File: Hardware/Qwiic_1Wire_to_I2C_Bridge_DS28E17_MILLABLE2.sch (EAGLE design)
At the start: 20 parts, among them J1 RJ45, J2 RJ45, J3 RJ11, J4 RJ11

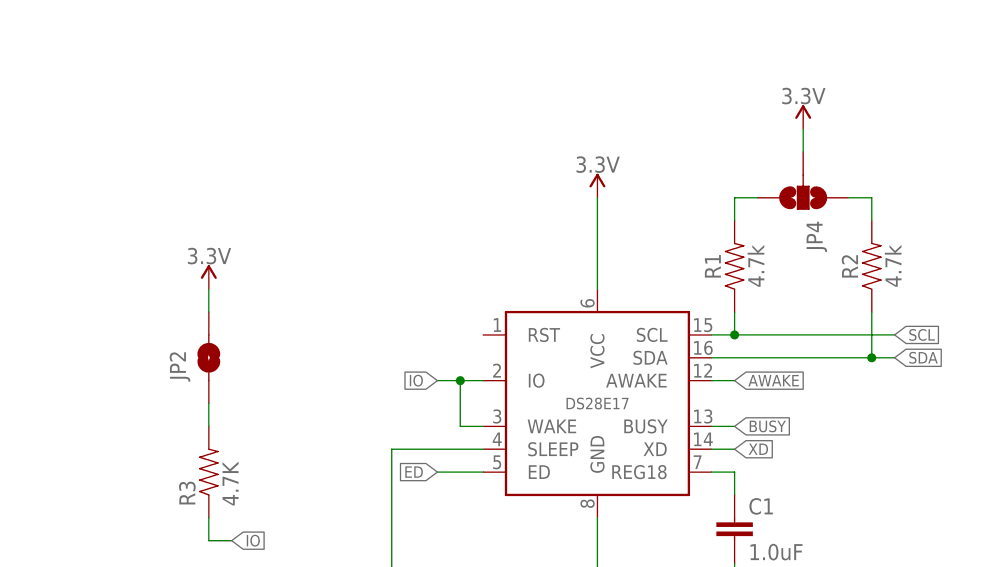
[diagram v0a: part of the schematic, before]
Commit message: Routed more on production layout
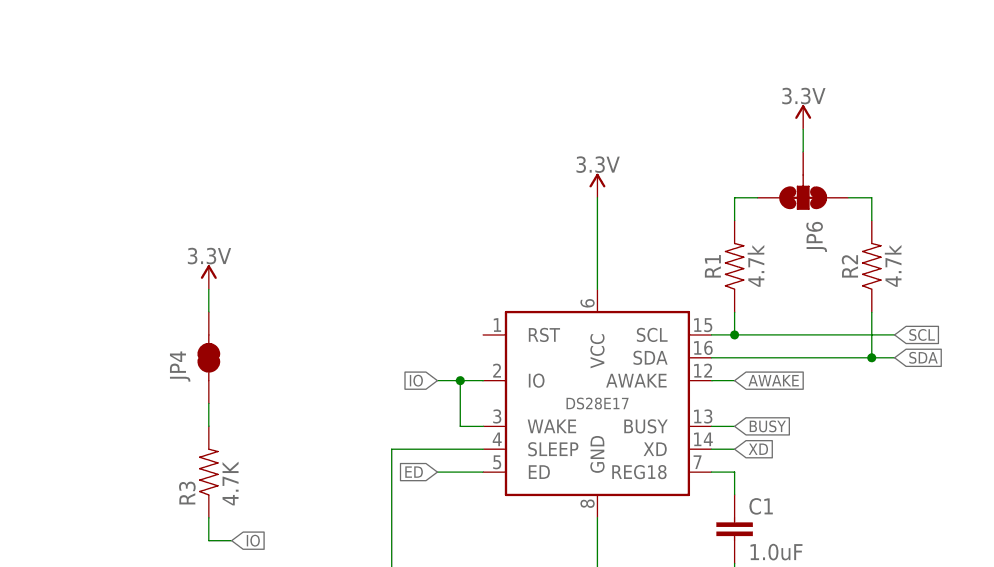
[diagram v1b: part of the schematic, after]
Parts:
- removed JP2: JUMPER-SMT_2_NO_NO-SILK, SparkFun-Jumpers:JUMPER-SMT_2_NO_NO-SILK
- added JP6: JUMPER-SMT_3_2-NC_TRACE_NO-SILK, SparkFun-Jumpers:JUMPER-SMT_3_2-NC_TRACE_NO-SILK
- JP4: value JUMPER-SMT_3_NO_NO-SILK -> JUMPER-SMT_2_NC_TRACE_NO-SILK; device SparkFun-Jumpers:JUMPER-SMT_3_NO_NO-SILK -> SparkFun-Jumpers:JUMPER-SMT_2_NC_TRACE_NO-SILK
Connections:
- net 3.3V: now also JP6.2; no longer JP2.2
- net N$2: now also JP4.1; no longer JP2.1
- net N$3: now also JP6.1; no longer JP4.1
- net N$4: now also JP6.3; no longer JP4.3
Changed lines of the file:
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@@
 <part name="R3" library="SparkFun-Resistors" deviceset="4.7KOHM-1/10W-1%(0603)" device="" value="4.7K"/>
 <part name="P+1" library="SparkFun" deviceset="VCC" device="" value="3.3V"/>
+<part name="JP4" library="SparkFun-Jumpers" deviceset="JUMPER-SMT_2_NC_TRACE" device="_NO-SILK" value=""/>
 <part name="SUPPLY4" library="SparkFun-PowerSymbols" deviceset="3.3V" device=""/>
 <part name="SUPPLY5" library="SparkFun-PowerSymbols" deviceset="3.3V" device=""/>
+<part name="JP6" library="SparkFun-Jumpers" deviceset="JUMPER-SMT_3_2-NC_TRACE" device="_NO-SILK" value=""/>
 <part name="J1" library="SparkFun-Connectors" deviceset="RJ45-8" device="" value="RJ45"/>
 <part name="J3" library="SparkFun-Connectors" deviceset="RJ11-6" device="" value="RJ11"/>
@@
 <part name="GND7" library="SparkFun-PowerSymbols" deviceset="GND" device=""/>
 <part name="SUPPLY3" library="SparkFun-PowerSymbols" deviceset="3.3V" device=""/>
-<part name="JP2" library="SparkFun-Jumpers" deviceset="JUMPER-SMT_2_NO" device="_NO-SILK" value=""/>
-<part name="JP4" library="SparkFun-Jumpers" deviceset="JUMPER-SMT_3_NO" device="_NO-SILK" value=""/>
 </parts>
 <sheets>
@@
 <instance part="R3" gate="G$1" x="78.74" y="114.3" rot="R90"/>
 <instance part="P+1" gate="1" x="45.72" y="127"/>
+<instance part="JP4" gate="G$1" x="78.74" y="127" rot="R90"/>
 <instance part="SUPPLY4" gate="G$1" x="78.74" y="134.62"/>
 <instance part="SUPPLY5" gate="G$1" x="144.78" y="152.4"/>
+<instance part="JP6" gate="G$1" x="144.78" y="144.78" rot="R270"/>
 <instance part="J1" gate="JP1" x="25.4" y="119.38" rot="R180"/>
 <instance part="J3" gate="G$1" x="17.78" y="96.52"/>
@@
 <instance part="GND7" gate="1" x="190.5" y="55.88"/>
 <instance part="SUPPLY3" gate="G$1" x="190.5" y="73.66"/>
-<instance part="JP2" gate="G$1" x="78.74" y="127" rot="R90"/>
-<instance part="JP4" gate="G$1" x="144.78" y="144.78" rot="R270"/>
 </instances>
 <busses>
@@
 </segment>
 <segment>
+<pinref part="JP4" gate="G$1" pin="2"/>
 <pinref part="SUPPLY4" gate="G$1" pin="3.3V"/>
 <wire x1="78.74" y1="134.62" x2="78.74" y2="132.08" width="0.1524" layer="91"/>
-<pinref part="JP2" gate="G$1" pin="2"/>
 </segment>
 <segment>
@@
 <pinref part="SUPPLY5" gate="G$1" pin="3.3V"/>
 <wire x1="144.78" y1="152.4" x2="144.78" y2="149.86" width="0.1524" layer="91"/>
-<pinref part="JP4" gate="G$1" pin="2"/>
+<pinref part="JP6" gate="G$1" pin="2"/>
 </segment>
 <segment>
@@
 <net name="N$2" class="0">
 <segment>
+<pinref part="JP4" gate="G$1" pin="1"/>
 <pinref part="R3" gate="G$1" pin="2"/>
 <wire x1="78.74" y1="119.38" x2="78.74" y2="121.92" width="0.1524" layer="91"/>
-<pinref part="JP2" gate="G$1" pin="1"/>
 </segment>
 </net>
@@
 <wire x1="152.4" y1="142.24" x2="152.4" y2="144.78" width="0.1524" layer="91"/>
 <wire x1="152.4" y1="144.78" x2="149.86" y2="144.78" width="0.1524" layer="91"/>
-<pinref part="JP4" gate="G$1" pin="1"/>
+<pinref part="JP6" gate="G$1" pin="1"/>
 </segment>
 </net>
@@
 <wire x1="137.16" y1="142.24" x2="137.16" y2="144.78" width="0.1524" layer="91"/>
 <wire x1="137.16" y1="144.78" x2="139.7" y2="144.78" width="0.1524" layer="91"/>
-<pinref part="JP4" gate="G$1" pin="3"/>
-</segment>
-</net>
+<pinref part="JP6" gate="G$1" pin="3"/>
+</segment>
+</net>

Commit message: MIllable version 2
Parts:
- removed JP1: (no value), SparkX:I2C_STANDARDSILK
- removed JP4: JUMPER-SMT_2_NC_TRACE_NO-SILK, SparkFun-Jumpers:JUMPER-SMT_2_NC_TRACE_NO-SILK
- removed JP5: (no value), SparkX:I2C_STANDARDJS-1MM
- removed JP6: JUMPER-SMT_3_2-NC_TRACE_NO-SILK, SparkFun-Jumpers:JUMPER-SMT_3_2-NC_TRACE_NO-SILK
- added JP2: JUMPER-SMT_2_NO_NO-SILK, SparkFun-Jumpers:JUMPER-SMT_2_NO_NO-SILK
- added JP7: JUMPER-SMT_3_NO_NO-SILK, SparkFun-Jumpers:JUMPER-SMT_3_NO_NO-SILK
- added TP1, TP2: TEST-POINT3X4, SparkFun-Connectors:TEST-POINT3X4
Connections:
- new net N$5: JP3.SCL, TP1.1
- new net N$6: JP3.SDA, TP2.1
- net 3.3V: now also JP2.2, JP7.2; no longer JP1.VCC, JP4.2, JP5.VCC, JP6.2
- net GND: no longer JP1.GND, JP5.GND
- net N$2: now also JP2.1; no longer JP4.1
- net N$3: now also JP7.1; no longer JP6.1
- net N$4: now also JP7.3; no longer JP6.3
- net SCL: no longer JP1.SCL, JP3.SCL, JP5.SCL
- net SDA: no longer JP1.SDA, JP3.SDA, JP5.SDA
